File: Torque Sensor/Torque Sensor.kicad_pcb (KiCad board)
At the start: 2 copper layers, 23 parts, among them J2 Full Bridge Strain Guage, U3 AD7173-8

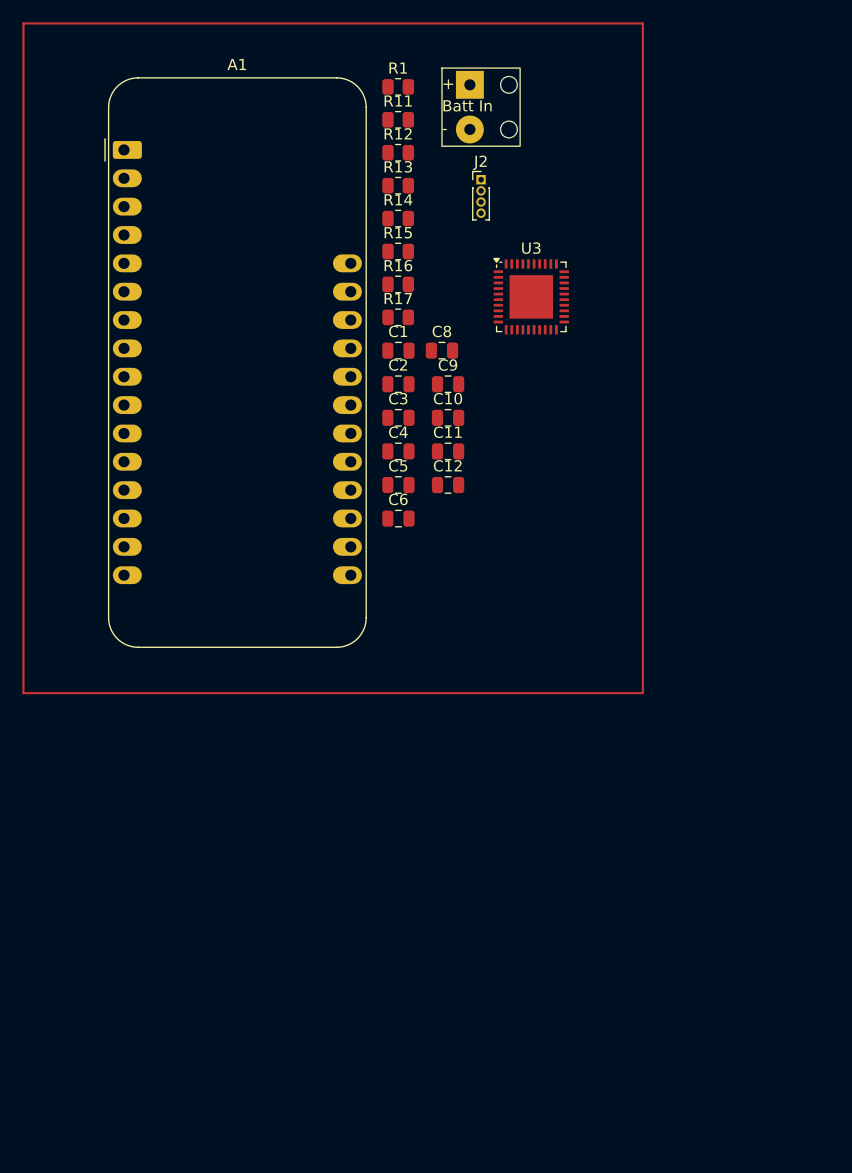
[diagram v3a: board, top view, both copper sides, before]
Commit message: Designed PCB for torque sensor
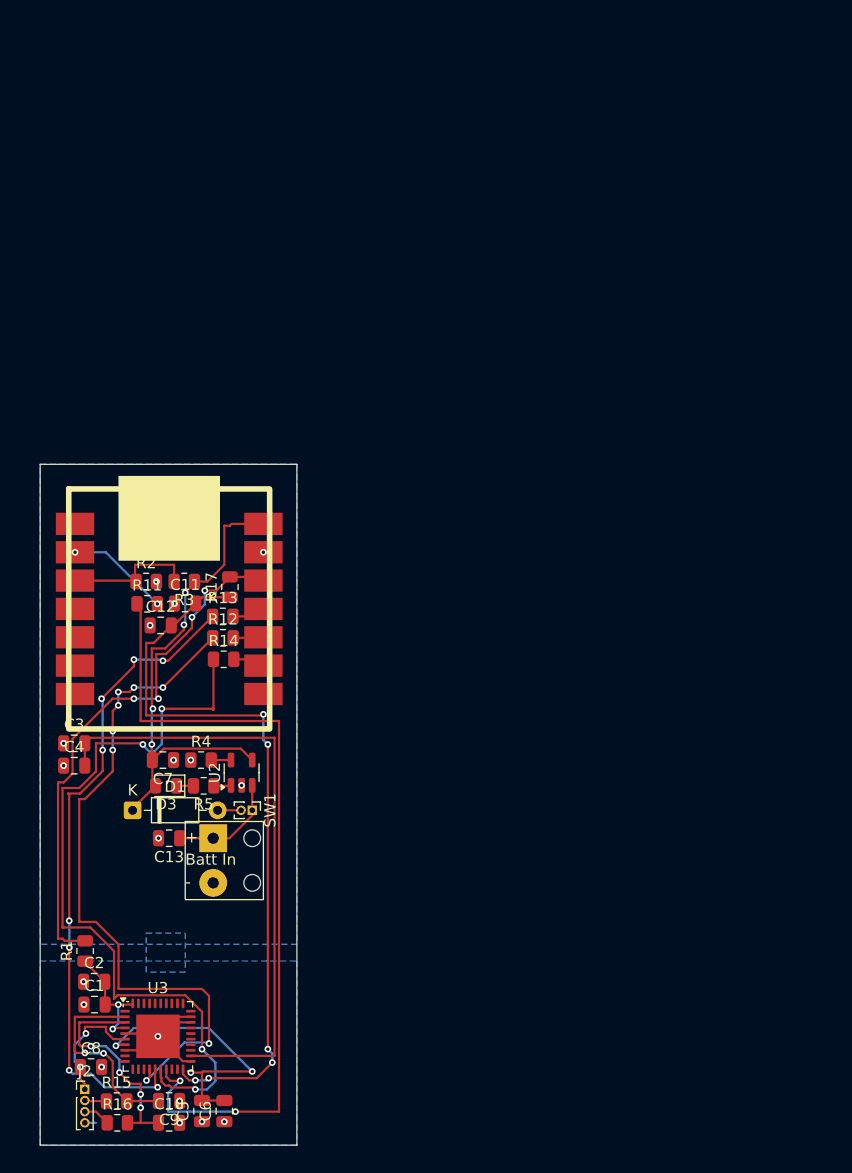
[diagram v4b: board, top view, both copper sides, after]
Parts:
- removed A1: Adafruit_Feather_Generic, Module:Adafruit_Feather
- added C13: 10uF 16V, Capacitor_SMD:C_0805_2012Metric, F.Cu at (131.1, 131.5)
- added C7: 10uF 16V, Capacitor_SMD:C_0805_2012Metric, F.Cu at (130.5, 124.5)
- added D1: ~, Diode_THT:D_DO-35_SOD27_P7.62mm_Horizontal, F.Cu at (127.8, 129.0)
- added D3: LED, LED_SMD:LED_0805_2012Metric, F.Cu at (130.8, 126.8)
- added R2: 100kR, Resistor_SMD:R_0805_2012Metric, F.Cu at (129.0, 108.5)
- added R3: 100kR, Resistor_SMD:R_0805_2012Metric, F.Cu at (132.4, 108.5)
- added R4: 5.1kR, Resistor_SMD:R_0805_2012Metric, F.Cu at (133.9, 124.5)
- added R5: 1kR, Resistor_SMD:R_0805_2012Metric, F.Cu at (134.1, 126.8)
- added SW1: SCREW, Connector_PinHeader_1.00mm:PinHeader_1x02_P1.00mm_Vertical, F.Cu at (138.5, 129.0)
- added U2: MCP73831-2-OT, Package_TO_SOT_SMD:SOT-23-5, F.Cu at (137.5, 125.6)
- added U4: ~, TestLib:Adafruit QT PY, F.Cu at (123.4, 103.3)
- moved J2 88.9 mm to (123.5, 154.0)
- moved R1 82.3 mm to (123.5, 141.6), turned to 90 degrees
- moved R15 80.2 mm to (126.4, 155.0)
- moved R16 79.2 mm to (126.4, 157.0)
- moved U3 74.2 mm to (130.1, 149.2)
- moved C8 71.5 mm to (124.0, 152.0)
- moved U1 71.3 mm to (135.0, 132.0)
- moved C9 68.9 mm to (131.1, 155.0), turned to 180 degrees
- moved C10 67.9 mm to (131.1, 157.0)
- moved C1 64.6 mm to (124.4, 146.4)
- moved C2 60.1 mm to (124.3, 144.4)
- moved C5 58.8 mm to (134.0, 155.9), turned to 90 degrees
- moved C6 55.3 mm to (136.0, 155.9), turned to 90 degrees
- moved R11 48.8 mm to (129.1, 110.5)
- moved R12 46.2 mm to (135.9, 113.5)
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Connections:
- U3 pad 22: GND -> Net-(U3-REGCAPD)
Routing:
- net Net-(U3-CS): track 0.00 -> 73.2 mm, vias 0 -> 2
- net Net-(U3-SCLK): track 0.00 -> 69.1 mm, vias 0 -> 4
- net Net-(U3-IOVDD): track 0.00 -> 67.1 mm, vias 0 -> 6
- net Net-(U3-DOUT/RDY): track 0.00 -> 62.0 mm, vias 0 -> 8
- net Net-(U3-DIN): track 0.00 -> 59.0 mm, vias 0 -> 8
- net Net-(U3-REGCAPD): track 0.00 -> 55.2 mm
- net +3.3V: track 0.00 -> 48.4 mm, vias 0 -> 4
- net +5V: track 0.00 -> 44.0 mm, vias 0 -> 4
- net Net-(U3-REGCAPA): track 0.00 -> 25.4 mm, vias 0 -> 3
- net Net-(U3-AIN1/REF2+): track 0.00 -> 20.3 mm, vias 0 -> 4
- net GND: track 0.00 -> 19.2 mm, vias 0 -> 19
- net Net-(U3-AIN0/REF2-): track 0.00 -> 18.3 mm, vias 0 -> 2
- net CHRG_IND: track 0.00 -> 12.0 mm
- net Net-(J2-Pin_1): track 0.00 -> 10.7 mm, vias 0 -> 2
- net AVDD: track 0.00 -> 10.7 mm, vias 0 -> 2
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- added copper zone on B.Cu, net GND
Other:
- board outline added: 23 x 61 mm

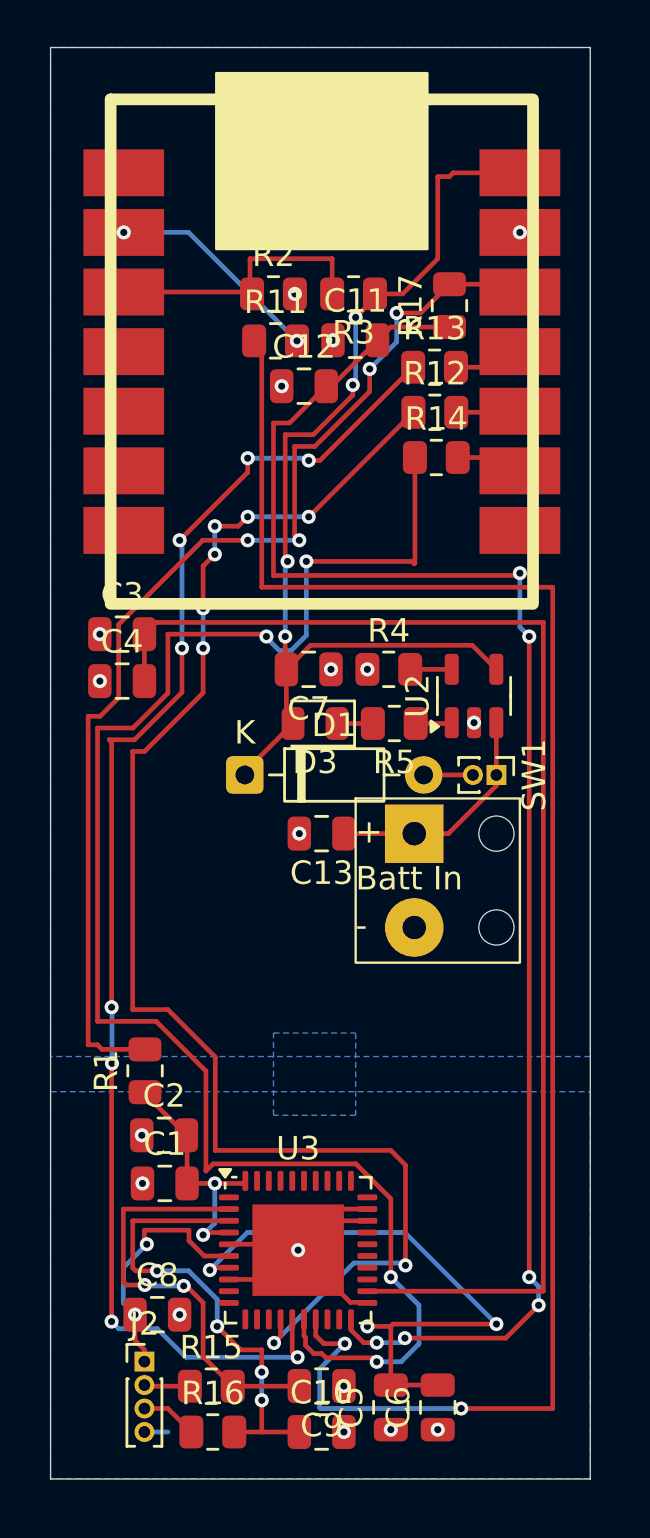
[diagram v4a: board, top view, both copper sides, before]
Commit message: flipped QTPY to back
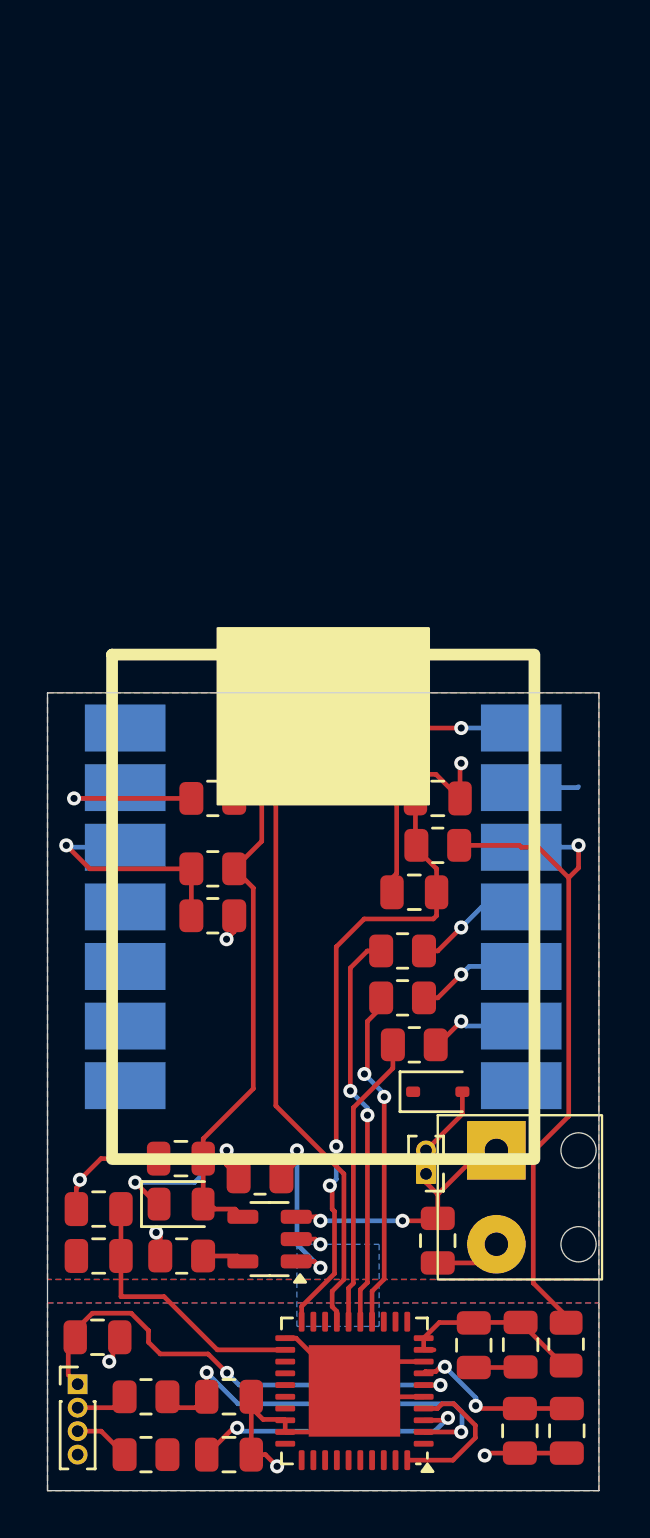
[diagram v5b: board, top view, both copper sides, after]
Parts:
- D1: footprint Diode_THT:D_DO-35_SOD27_P7.62mm_Horizontal -> Diode_SMD:D_SOD-323
- moved R2 26.6 mm to (126.4, 135.0)
- moved R4 26.5 mm to (125.1, 149.5)
- moved R3 25.2 mm to (126.4, 133.0)
- moved R14 25.0 mm to (135.0, 140.5)
- moved R12 25.0 mm to (134.5, 138.5)
- moved R13 24.9 mm to (134.5, 136.5)
- moved U2 24.7 mm to (128.8, 148.8), turned to 180 degrees
- moved C3 24.5 mm to (121.5, 147.5)
- moved C4 24.5 mm to (121.5, 149.5)
- moved U4 23.7 mm to (123.5, 127.0)
- moved R17 23.0 mm to (136.0, 132.0), turned to 0 degrees
- moved C12 22.1 mm to (135.0, 134.0)
- moved C7 21.5 mm to (125.1, 145.4), turned to 0 degrees
- moved R1 21.4 mm to (141.5, 153.3)
- moved D3 21.3 mm to (125.1, 147.3), turned to 0 degrees
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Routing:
- net Net-(U3-SCLK): track 69.1 -> 12.6 mm, vias 4 -> 0
- net Net-(U3-DOUT/RDY): track 62.0 -> 14.7 mm, vias 8 -> 2
- net Net-(U3-CS): track 73.2 -> 27.5 mm
- net Net-(U3-REGCAPD): track 55.2 -> 11.3 mm
- net Net-(U3-DIN): track 59.0 -> 17.1 mm, vias 8 -> 2
- net Net-(U3-IOVDD): track 67.1 -> 26.9 mm, vias 6 -> 2
- net GND: track 19.2 -> 52.9 mm, vias 19 -> 8
- net +3.3V: track 48.4 -> 29.4 mm, vias 4 -> 1
- net Net-(U3-REGCAPA): track 25.4 -> 7.17 mm, vias 3 -> 2
- net Net-(J2-Pin_1): track 10.7 -> 20.7 mm
- net +5V: track 44.0 -> 34.7 mm, vias 4 -> 1
- net Net-(U3-AIN1/REF2+): track 20.3 -> 12.1 mm, vias 4 -> 2
- net Net-(U2-STAT): track 1.55 -> 7.96 mm, vias 0 -> 2
- net Net-(D3-K): track 1.53 -> 7.20 mm, vias 0 -> 2
- net AVDD: track 10.7 -> 14.6 mm, vias 2 -> 0
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- added copper zone on F.Cu, net GND
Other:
- board size 23 x 61 mm -> 23.5 x 34 mm
